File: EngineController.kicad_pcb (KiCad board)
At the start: 4 copper layers, 16 parts, among them U3 LM66200DRLR, U4 MAX77827AEFD+T, U5 SC4215

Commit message: Completed schematics
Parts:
- added 12VLED1: RED_LED, Resistor_SMD:R_0402_1005Metric, F.Cu at (158.8, 71.8)
- added 3V3LED1: BLUE_LED, Resistor_SMD:R_0402_1005Metric, F.Cu at (158.8, 73.8)
- added BOOTJUMPER1: Conn_01x02_Male, Connector_PinHeader_2.54mm:PinHeader_1x02_P2.54mm_Vertical, F.Cu at (149.9, 82.4)
- added C1: 10uF, Capacitor_SMD:C_0402_1005Metric, F.Cu at (164.9, 58.7)
- added C10: 0.1uF, Capacitor_SMD:C_0402_1005Metric, F.Cu at (167.7, 66.6)
- added C11: 0.1uF, Capacitor_SMD:C_0402_1005Metric, F.Cu at (170.6, 58.7)
- added C12: 11pF, Capacitor_SMD:C_0402_1005Metric, F.Cu at (170.6, 60.7)
- added C13: 11pF, Capacitor_SMD:C_0402_1005Metric, F.Cu at (170.6, 62.7)
- added C14: 100nF, Capacitor_SMD:C_0402_1005Metric, F.Cu at (151.7, 127.2)
- added C15: 10uF, Capacitor_SMD:C_0402_1005Metric, F.Cu at (151.7, 129.2)
- added C16: 47nF, Capacitor_SMD:C_0402_1005Metric, F.Cu at (151.7, 131.1)
- added C2: 1uF, Capacitor_SMD:C_0402_1005Metric, F.Cu at (164.9, 60.7)
- added C25: 1uF, Capacitor_SMD:C_0402_1005Metric, F.Cu at (111.6, 97.8)
- added C26: 4.7uF, Capacitor_SMD:C_0402_1005Metric, F.Cu at (111.6, 99.7)
- added C27: 47uF, Capacitor_SMD:C_1206_3216Metric, F.Cu at (96.0, 98.4)
- added C28: 47uF, Capacitor_SMD:C_1206_3216Metric, F.Cu at (96.0, 101.8)
- added C29: 47uF, Capacitor_SMD:C_1206_3216Metric, F.Cu at (96.0, 105.1)
- added C3: 0.1uF, Capacitor_SMD:C_0402_1005Metric, F.Cu at (164.9, 62.7)
- added C30: DNP, Capacitor_SMD:C_1206_3216Metric, F.Cu at (96.0, 108.5)
- added C31: 47uF, Capacitor_SMD:C_1206_3216Metric, F.Cu at (96.0, 111.8)
- added C32: DNP, Capacitor_SMD:C_1206_3216Metric, F.Cu at (101.7, 98.4)
- added C33: 47uF, Capacitor_SMD:C_1206_3216Metric, F.Cu at (101.7, 101.8)
- added C34: 100nF, Capacitor_SMD:C_0402_1005Metric, F.Cu at (111.6, 101.7)
- added C35: 0.1uF, Capacitor_SMD:C_0402_1005Metric, F.Cu at (111.6, 103.7)
- added C36: DNP, Capacitor_SMD:C_1206_3216Metric, F.Cu at (101.7, 105.1)
- added C37: DNP, Capacitor_SMD:C_0805_2012Metric, F.Cu at (112.1, 115.0)
- added C38: DNP, Capacitor_SMD:C_1206_3216Metric, F.Cu at (101.7, 108.5)
- added C39: DNP, Capacitor_SMD:C_1206_3216Metric, F.Cu at (101.7, 111.8)
- added C4: 1uF, Capacitor_SMD:C_0402_1005Metric, F.Cu at (164.9, 64.6)
- added C40: DNP, Capacitor_SMD:C_1206_3216Metric, F.Cu at (107.3, 98.4)
- added C41: DNP, Capacitor_SMD:C_0805_2012Metric, F.Cu at (112.1, 118.0)
- added C42: DNP, Capacitor_SMD:C_1206_3216Metric, F.Cu at (107.3, 101.8)
- added C43: DNP, Capacitor_SMD:C_1206_3216Metric, F.Cu at (107.3, 105.1)
- added C44: DNP, Capacitor_SMD:C_1206_3216Metric, F.Cu at (107.3, 108.5)
- added C45: DNP, Capacitor_SMD:C_1206_3216Metric, F.Cu at (107.3, 111.8)
- added C46: 0.1uF, Capacitor_SMD:C_0402_1005Metric, F.Cu at (155.6, 101.7)
- added C47: 1uF, Capacitor_SMD:C_0402_1005Metric, F.Cu at (114.2, 74.5)
- added C48: 220nF, Capacitor_SMD:C_0402_1005Metric, F.Cu at (114.2, 76.4)
- added C49: 10uF, Capacitor_SMD:C_0603_1608Metric, F.Cu at (130.7, 74.7)
- added C5: 0.1uF, Capacitor_SMD:C_0402_1005Metric, F.Cu at (164.9, 66.6)
- added C50: 0.1uF, Capacitor_SMD:C_0402_1005Metric, F.Cu at (114.2, 78.4)
- added C51: 0.1uF, Capacitor_SMD:C_0402_1005Metric, F.Cu at (114.2, 80.4)
- added C52: 100nF, Capacitor_SMD:C_0603_1608Metric, F.Cu at (130.7, 77.2)
- added C53: 10nF, Capacitor_SMD:C_0402_1005Metric, F.Cu at (114.2, 82.3)
- added C54: 10nF, Capacitor_SMD:C_0402_1005Metric, F.Cu at (114.2, 84.3)
- added C55: 10nF, Capacitor_SMD:C_0402_1005Metric, F.Cu at (114.2, 86.3)
- added C56: 10uF, Capacitor_SMD:C_0603_1608Metric, F.Cu at (136.7, 108.0)
- added C57: 180pF, Capacitor_SMD:C_0402_1005Metric, F.Cu at (117.8, 97.8)
- added C58: 3.9nF, Capacitor_SMD:C_0402_1005Metric, F.Cu at (117.8, 99.7)
- added C59: 1uF, Capacitor_SMD:C_0402_1005Metric, F.Cu at (117.8, 101.7)
- added C6: 0.1uF, Capacitor_SMD:C_0402_1005Metric, F.Cu at (167.7, 58.7)
- added C60: 22uF, Capacitor_SMD:C_0805_2012Metric, F.Cu at (127.2, 108.2)
- added C61: 22uF, Capacitor_SMD:C_0805_2012Metric, F.Cu at (127.2, 111.2)
- added C62: 100nF, Capacitor_SMD:C_0402_1005Metric, F.Cu at (117.8, 103.7)
- added C63: 2.2uF, Capacitor_SMD:C_0402_1005Metric, F.Cu at (117.8, 105.6)
- added C64: 100nF, Capacitor_SMD:C_0402_1005Metric, F.Cu at (117.8, 107.6)
- added C65: 47uF, Capacitor_SMD:C_1206_3216Metric, F.Cu at (119.2, 110.3)
- added C66: 10uF, Capacitor_SMD:C_0402_1005Metric, F.Cu at (120.6, 97.8)
- added C67: 100nF, Capacitor_SMD:C_0402_1005Metric, F.Cu at (120.6, 99.7)
- added C68: 10uF, Capacitor_SMD:C_0603_1608Metric, F.Cu at (136.7, 110.5)
- added C69: 1uF, Capacitor_SMD:C_0402_1005Metric, F.Cu at (120.6, 101.7)
- added C7: 1uF, Capacitor_SMD:C_0402_1005Metric, F.Cu at (167.7, 60.7)
- added C70: 120pF, Capacitor_SMD:C_0402_1005Metric, F.Cu at (120.6, 103.7)
- added C71: 2.2nF, Capacitor_SMD:C_0805_2012Metric, F.Cu at (127.2, 114.2)
- added C72: 22uF, Capacitor_SMD:C_0805_2012Metric, F.Cu at (127.2, 117.3)
- added C73: 2.2uF, Capacitor_SMD:C_0402_1005Metric, F.Cu at (120.6, 105.6)
- added C74: 100nF, Capacitor_SMD:C_0402_1005Metric, F.Cu at (120.6, 107.6)
- added C75: 100nF, Capacitor_SMD:C_0402_1005Metric, F.Cu at (123.5, 97.8)
- added C76: 22uF, Capacitor_SMD:C_1206_3216Metric, F.Cu at (119.2, 113.6)
- added C77: 10uF, Capacitor_SMD:C_0402_1005Metric, F.Cu at (123.5, 99.7)
- added C78: 100nF, Capacitor_SMD:C_0402_1005Metric, F.Cu at (123.5, 101.7)
- added C8: 0.1uF, Capacitor_SMD:C_0402_1005Metric, F.Cu at (167.7, 62.7)
- added C9: 10nF, Capacitor_SMD:C_0402_1005Metric, F.Cu at (167.7, 64.6)
- added D1: SM712_SOT23, Package_TO_SOT_SMD:SOT-23, F.Cu at (155.5, 128.4)
- added D2: SP0503BAHT, Package_TO_SOT_SMD:SOT-143, F.Cu at (161.2, 109.0)
- added ENJUMPER1: Conn_01x02_Male, Connector_PinHeader_2.54mm:PinHeader_1x02_P2.54mm_Vertical, F.Cu at (154.6, 82.4)
- added H1: MountingHole_Pad, MountingHole:MountingHole_3.2mm_M3_DIN965_Pad, F.Cu at (144.0, 61.3)
- added H2: MountingHole_Pad, MountingHole:MountingHole_3.2mm_M3_DIN965_Pad, F.Cu at (144.0, 68.5)
- added H3: MountingHole_Pad, MountingHole:MountingHole_3.2mm_M3_DIN965_Pad, F.Cu at (144.0, 75.6)
- added H4: MountingHole_Pad, MountingHole:MountingHole_3.2mm_M3_DIN965_Pad, F.Cu at (144.0, 82.8)
- added IC1: TPS61089RNRR, iclr:IC_TPS61089RNRR, F.Cu at (136.4, 98.8)
- added IC2: AP2205-W5-7, iclr:SOT95P282X145-5N, F.Cu at (132.0, 109.0)
- added IC3: AP2205-W5-7, iclr:SOT95P282X145-5N, F.Cu at (132.0, 113.7)
- added IC4: TPS61089RNRR, iclr:IC_TPS61089RNRR, F.Cu at (136.4, 102.8)
- added J1: RBUS, Connector_Molex:Molex_Mini-Fit_Jr_5566-06A_2x03_P4.20mm_Vertical, F.Cu at (151.3, 61.0)
- added J2: USB_C_Receptacle_USB2.0, Connector_USB:USB_C_Receptacle_Palconn_UTC16-G, F.Cu at (164.9, 100.9)
- added J3: ServoCH1, Connector_Molex:Molex_Nano-Fit_105313-xx03_1x03_P2.50mm_Horizontal, F.Cu at (142.8, 99.5)
- added J4: ServoCH2, Connector_Molex:Molex_Nano-Fit_105313-xx03_1x03_P2.50mm_Horizontal, F.Cu at (142.8, 110.0)
- added J5: 1053131104, iclr:1053131104, F.Cu at (104.2, 59.8)
- added J6: 1053131104, iclr:1053131104, F.Cu at (119.3, 59.8)
- added J7: 1053131104, iclr:1053131104, F.Cu at (134.4, 59.8)
- added JP1: TermJP, Jumper:SolderJumper-2_P1.3mm_Open_RoundedPad1.0x1.5mm, F.Cu at (156.8, 121.5)
- added JP10: SolderJumper_3_Open, Jumper:SolderJumper-3_P1.3mm_Open_RoundedPad1.0x1.5mm_NumberLabels, F.Cu at (96.0, 93.0)
- added JP2: SolderJumper_3_Open, Jumper:SolderJumper-3_P1.3mm_Open_RoundedPad1.0x1.5mm_NumberLabels, F.Cu at (96.0, 75.2)
- added JP3: SolderJumper_2_Open, Jumper:SolderJumper-2_P1.3mm_Open_RoundedPad1.0x1.5mm, F.Cu at (126.6, 75.2)
- added JP4: SolderJumper_3_Open, Jumper:SolderJumper-3_P1.3mm_Open_RoundedPad1.0x1.5mm_NumberLabels, F.Cu at (96.0, 78.8)
- added JP5: SolderJumper_3_Open, Jumper:SolderJumper-3_P1.3mm_Open_RoundedPad1.0x1.5mm_NumberLabels, F.Cu at (96.0, 82.3)
- added JP6: SolderJumper_2_Open, Jumper:SolderJumper-2_P1.3mm_Open_RoundedPad1.0x1.5mm, F.Cu at (126.6, 78.8)
- added JP7: SolderJumper_3_Open, Jumper:SolderJumper-3_P1.3mm_Open_RoundedPad1.0x1.5mm_NumberLabels, F.Cu at (96.0, 85.9)
- added JP8: SolderJumper_3_Open, Jumper:SolderJumper-3_P1.3mm_Open_RoundedPad1.0x1.5mm_NumberLabels, F.Cu at (96.0, 89.4)
- added JP9: SolderJumper_2_Open, Jumper:SolderJumper-2_P1.3mm_Open_RoundedPad1.0x1.5mm, F.Cu at (126.6, 82.3)
- added L1: 2.0nH, Inductor_SMD:L_0402_1005Metric, F.Cu at (158.8, 75.8)
- added L2: 20nH, Inductor_SMD:L_0402_1005Metric, F.Cu at (158.8, 77.7)
- added Q1: SSM3K15AMFV,L3F, Package_TO_SOT_SMD:SOT-723, F.Cu at (111.6, 106.1)
- added R1: 10K, Resistor_SMD:R_0402_1005Metric, F.Cu at (158.8, 79.7)
- added R10: 60, Resistor_SMD:R_0603_1608Metric, F.Cu at (148.2, 130.0)
- added R11: 60, Resistor_SMD:R_0603_1608Metric, F.Cu at (148.2, 132.5)
- added R12: 5.1k, Resistor_SMD:R_0402_1005Metric, F.Cu at (167.8, 107.7)
- added R13: 5.1k, Resistor_SMD:R_0402_1005Metric, F.Cu at (167.8, 109.7)
- added R14: 5.1k, Resistor_SMD:R_0402_1005Metric, F.Cu at (167.8, 111.7)
- added R19: 10k, Resistor_SMD:R_0402_1005Metric, F.Cu at (94.7, 114.5)
- added R2: 470, Resistor_SMD:R_0402_1005Metric, F.Cu at (161.7, 71.8)
- added R20: 113k, Resistor_SMD:R_0402_1005Metric, F.Cu at (94.7, 116.5)
- added R21: 10k, Resistor_SMD:R_0402_1005Metric, F.Cu at (94.7, 118.5)
- added R22: 2.2, Resistor_SMD:R_0402_1005Metric, F.Cu at (97.6, 114.5)
- added R23: 442k, Resistor_SMD:R_0402_1005Metric, F.Cu at (97.6, 116.5)
- added R24: 1k, Resistor_SMD:R_0402_1005Metric, F.Cu at (97.6, 118.5)
- added R25: 200k, Resistor_SMD:R_0402_1005Metric, F.Cu at (100.5, 114.5)
- added R26: 100k, Resistor_SMD:R_0402_1005Metric, F.Cu at (100.5, 116.5)
- added R27: 10k, Resistor_SMD:R_0402_1005Metric, F.Cu at (100.5, 118.5)
- added R28: 1.5k, Resistor_SMD:R_0402_1005Metric, F.Cu at (155.6, 97.8)
- added R29: 470, Resistor_SMD:R_0402_1005Metric, F.Cu at (155.6, 99.8)
- added R3: 10K, Resistor_SMD:R_0402_1005Metric, F.Cu at (161.7, 73.8)
- added R30: 113k, Resistor_SMD:R_0402_1005Metric, F.Cu at (117.1, 74.5)
- added R31: 40.2k, Resistor_SMD:R_0402_1005Metric, F.Cu at (117.1, 76.5)
- added R32: 1k, Resistor_SMD:R_0402_1005Metric, F.Cu at (117.1, 78.4)
- added R33: 1k, Resistor_SMD:R_0402_1005Metric, F.Cu at (117.1, 80.4)
- added R34: 49k, Resistor_SMD:R_0402_1005Metric, F.Cu at (117.1, 82.4)
- added R35: 113k, Resistor_SMD:R_0402_1005Metric, F.Cu at (117.1, 84.4)
- added R36: 40.2k, Resistor_SMD:R_0402_1005Metric, F.Cu at (120.0, 74.5)
- added R37: 1k, Resistor_SMD:R_0402_1005Metric, F.Cu at (120.0, 76.5)
- added R38: 1k, Resistor_SMD:R_0402_1005Metric, F.Cu at (120.0, 78.4)
- added R39: 49k, Resistor_SMD:R_0402_1005Metric, F.Cu at (120.0, 80.4)
- added R4: 470, Resistor_SMD:R_0402_1005Metric, F.Cu at (161.7, 75.8)
- added R40: 113k, Resistor_SMD:R_0402_1005Metric, F.Cu at (120.0, 82.4)
- added R41: 40.2k, Resistor_SMD:R_0402_1005Metric, F.Cu at (120.0, 84.4)
- added R42: 1k, Resistor_SMD:R_0402_1005Metric, F.Cu at (122.9, 74.5)
- added R43: 1k, Resistor_SMD:R_0402_1005Metric, F.Cu at (122.9, 76.5)
- added R44: 49k, Resistor_SMD:R_0402_1005Metric, F.Cu at (122.9, 78.4)
- added R45: 7.87k, Resistor_SMD:R_0402_1005Metric, F.Cu at (126.4, 97.8)
- added R46: 360k, Resistor_SMD:R_0402_1005Metric, F.Cu at (126.4, 99.8)
- added R47: 100k, Resistor_SMD:R_0402_1005Metric, F.Cu at (126.4, 101.7)
- added R48: 560k, Resistor_SMD:R_0402_1005Metric, F.Cu at (126.4, 103.7)
- added R49: 50k, Resistor_SMD:R_0402_1005Metric, F.Cu at (126.4, 105.7)
- added R5: 499R, Resistor_SMD:R_0402_1005Metric, F.Cu at (161.7, 77.7)
- added R50: 152k, Resistor_SMD:R_0603_1608Metric, F.Cu at (136.7, 113.0)
- added R51: 309k, Resistor_SMD:R_0402_1005Metric, F.Cu at (129.3, 97.8)
- added R52: 18.7k, Resistor_SMD:R_0402_1005Metric, F.Cu at (129.3, 99.8)
- added R53: 976k, Resistor_SMD:R_0402_1005Metric, F.Cu at (129.3, 101.7)
- added R54: 100k, Resistor_SMD:R_0402_1005Metric, F.Cu at (129.3, 103.7)
- added R55: 51k, Resistor_SMD:R_0402_1005Metric, F.Cu at (129.3, 105.7)
- added R56: 442k, Resistor_SMD:R_0402_1005Metric, F.Cu at (132.2, 97.8)
- added R57: 475k, Resistor_SMD:R_0402_1005Metric, F.Cu at (132.2, 99.8)
- added R58: 287k, Resistor_SMD:R_0402_1005Metric, F.Cu at (132.2, 101.7)
- added R6: 3k, Resistor_SMD:R_0402_1005Metric, F.Cu at (161.7, 79.7)
- added R7: 1.5k, Resistor_SMD:R_0402_1005Metric, F.Cu at (164.6, 71.8)
- added R8: 2.2k, Resistor_SMD:R_0402_1005Metric, F.Cu at (164.6, 73.8)
- added R9: 0, Resistor_SMD:R_0603_1608Metric, F.Cu at (148.2, 127.5)
- added TP1: TestPoint, TestPoint:TestPoint_Pad_D1.0mm, F.Cu at (158.9, 82.3)
- added TP2: TestPoint, TestPoint:TestPoint_Pad_D1.0mm, F.Cu at (158.9, 85.3)
- added TP3: TestPoint, TestPoint:TestPoint_Pad_D1.0mm, F.Cu at (164.9, 108.3)
- added TP4: TestPoint, TestPoint:TestPoint_Pad_D1.0mm, F.Cu at (164.9, 111.3)
- added TP5: TestPoint, TestPoint:TestPoint_Pad_D1.5mm, F.Cu at (142.4, 121.5)
- added TP6: TestPoint, TestPoint:TestPoint_Pad_D1.5mm, F.Cu at (142.4, 125.1)
- added TP7: TestPoint, TestPoint:TestPoint_Pad_D1.5mm, F.Cu at (142.4, 128.6)
- added TP8: TestPoint, TestPoint:TestPoint_Pad_D1.5mm, F.Cu at (142.4, 132.2)
- added TXLED1: GREEN_LED, Resistor_SMD:R_0402_1005Metric, F.Cu at (164.6, 75.8)
- added U1: ESP32-S3, iclr:QFN40P700X700X90-57N, F.Cu at (152.7, 75.4)
- added U2: SN65HVD230, Package_SO:SOIC-8_3.9x4.9mm_P1.27mm, F.Cu at (150.4, 123.0)
- added U6: SiC437BED-T1-GE3, iclr:SiC437BEDT1GE3, F.Cu at (106.0, 117.4)
- added U7: ADS131M06IRSNR, iclr:ADS131M06IRSNR, F.Cu at (105.2, 81.1)
- added USBLED1: WHITE_LED, Resistor_SMD:R_0402_1005Metric, F.Cu at (167.8, 113.7)
- added Y1: R940000171, Crystal:Crystal_SMD_2016-4Pin_2.0x1.6mm, F.Cu at (162.3, 82.6)
- renumbered C20 to C17, C21 to C18, C22 to C19, C23 to C20, C24 to C21, C25 to C22, C26 to C23, C27 to C24, R14 to R15, R15 to R16, R16 to R17, R17 to R18

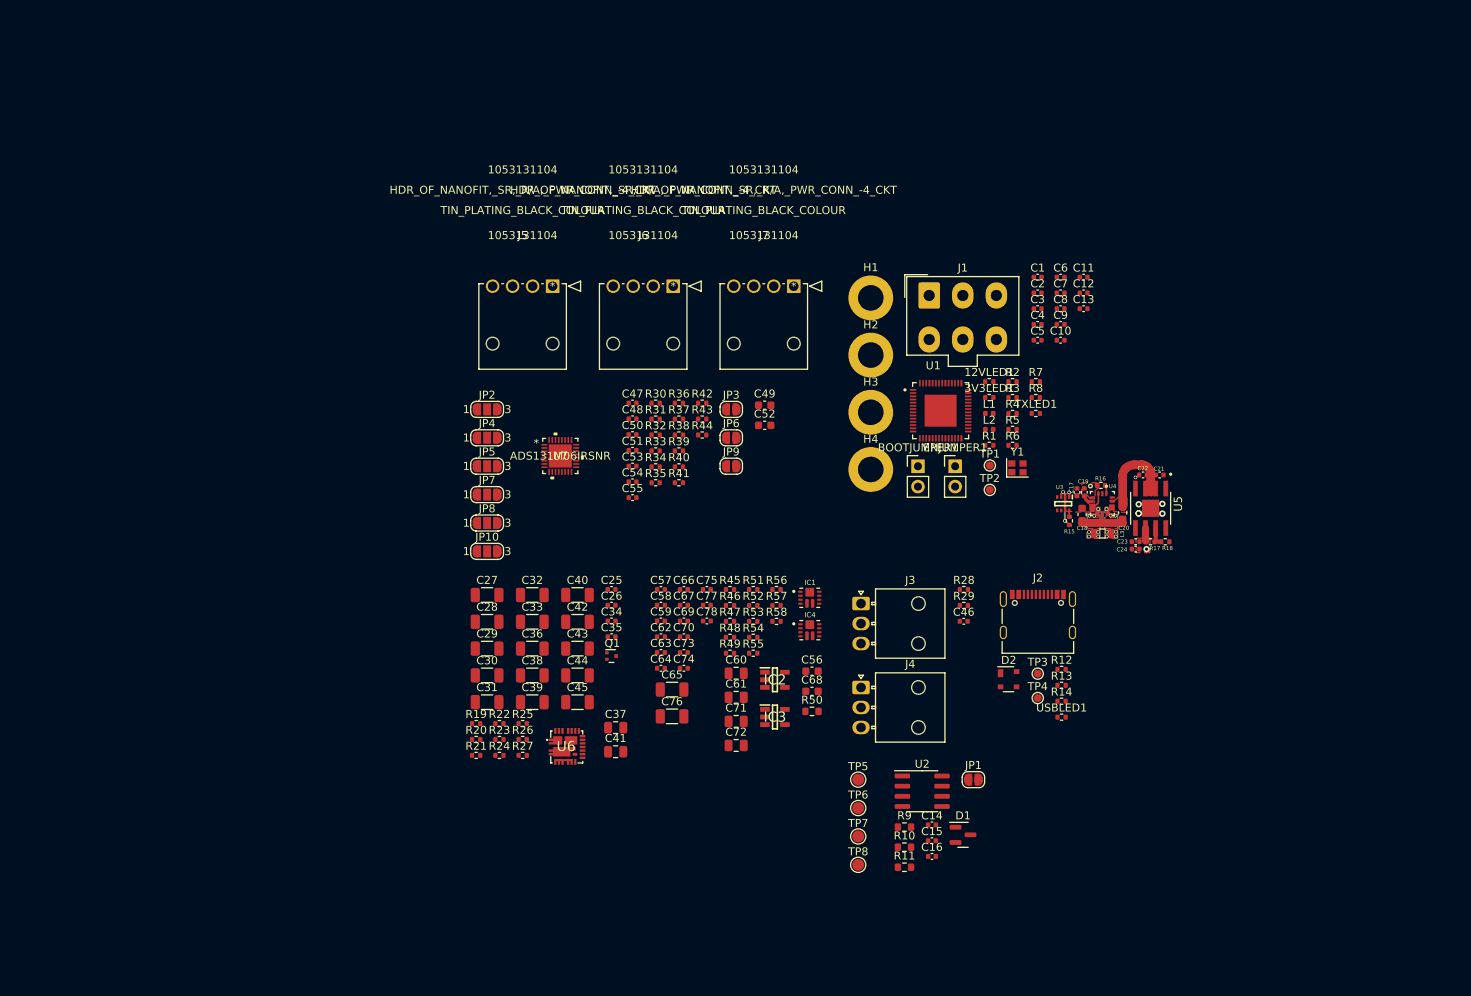
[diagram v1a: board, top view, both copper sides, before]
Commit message: forgot sd card and added ads chip
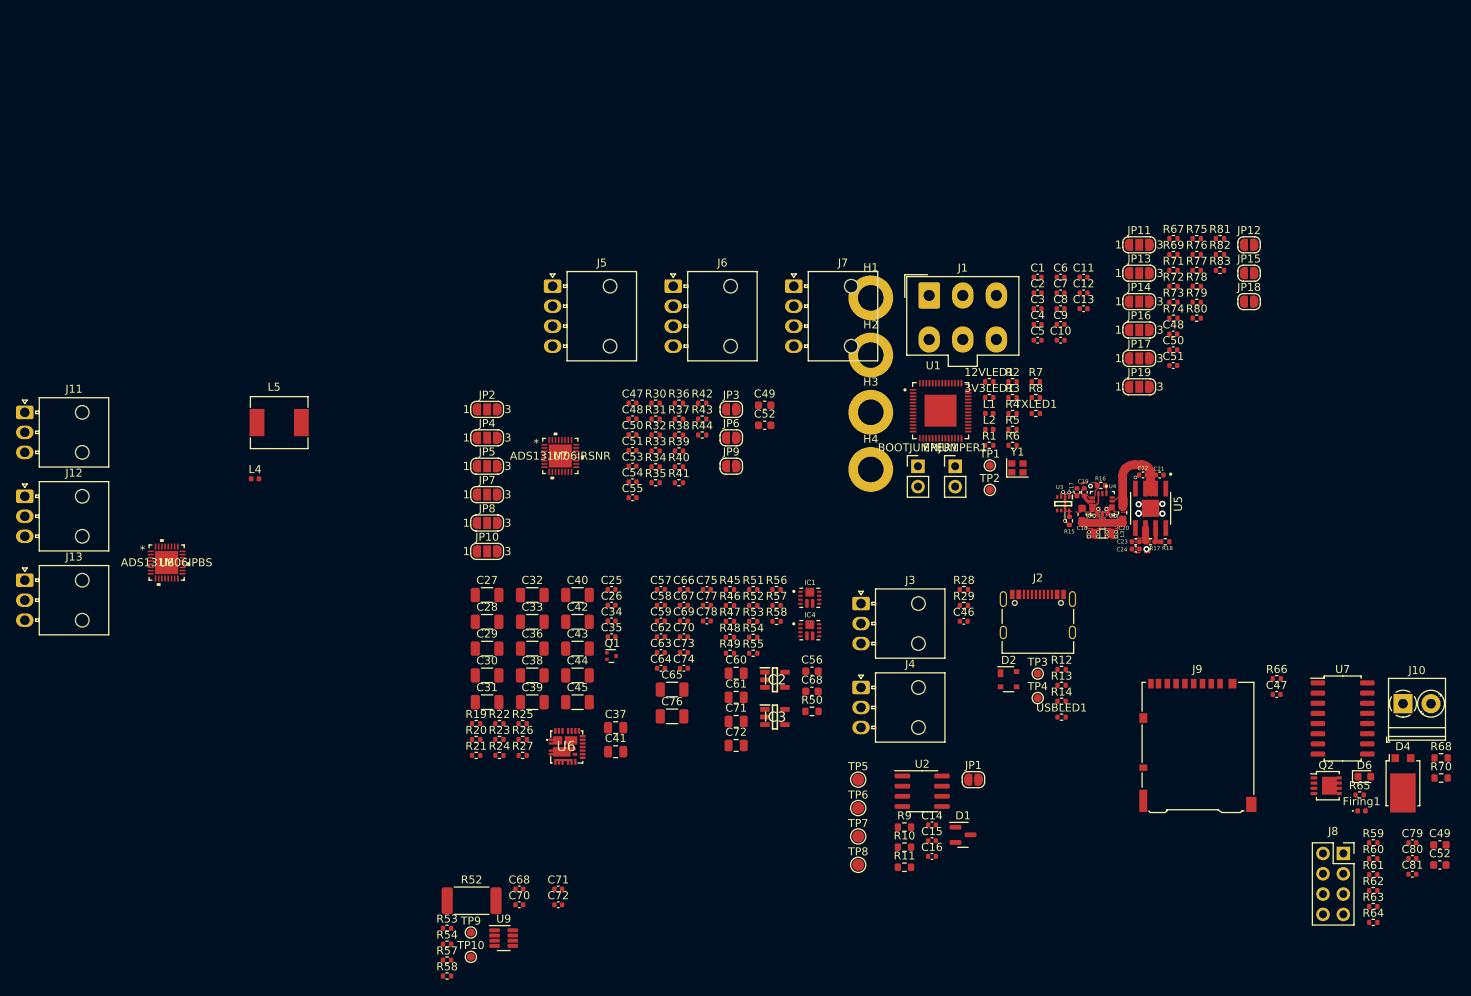
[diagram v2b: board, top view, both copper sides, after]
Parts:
- added C47: 0.1uF, Capacitor_SMD:C_0402_1005Metric, F.Cu at (194.7, 110.9)
- added C48: 10nF, Capacitor_SMD:C_0402_1005Metric, F.Cu at (181.8, 65.8)
- added C49: 10uF, Capacitor_SMD:C_0603_1608Metric, F.Cu at (215.1, 129.7)
- added C50: 10nF, Capacitor_SMD:C_0402_1005Metric, F.Cu at (181.8, 67.8)
- added C51: 10nF, Capacitor_SMD:C_0402_1005Metric, F.Cu at (181.8, 69.8)
- added C52: 100nF, Capacitor_SMD:C_0603_1608Metric, F.Cu at (215.1, 132.2)
- added C68: 0.1uF, Capacitor_SMD:C_0402_1005Metric, F.Cu at (100.1, 135.2)
- added C70: 0.1uF, Capacitor_SMD:C_0402_1005Metric, F.Cu at (100.1, 137.2)
- added C71: 1uF, Capacitor_SMD:C_0402_1005Metric, F.Cu at (104.9, 135.2)
- added C72: 1uF, Capacitor_SMD:C_0402_1005Metric, F.Cu at (104.9, 137.2)
- added C79: 1uF, Capacitor_SMD:C_0402_1005Metric, F.Cu at (211.7, 129.4)
- added C80: 1uF, Capacitor_SMD:C_0402_1005Metric, F.Cu at (211.7, 131.4)
- added C81: 220nF, Capacitor_SMD:C_0402_1005Metric, F.Cu at (211.7, 133.3)
- added D4: DST1550S, Package_TO_SOT_SMD:TO-277B, F.Cu at (210.5, 122.0)
- added D6: RED_LED, LED_SMD:LED_0603_1608Metric, F.Cu at (205.7, 121.2)
- added Firing1: EMERALD_LED, LED_SMD:LED_0402_1005Metric, F.Cu at (205.3, 125.4)
- added J10: Conn_01x02_Male, TerminalBlock_Phoenix:TerminalBlock_Phoenix_PT-1,5-2-3.5-H_1x02_P3.50mm_Horizontal, F.Cu at (210.5, 112.0)
- added J11: 1053131104, Connector_Molex:Molex_Nano-Fit_105313-xx03_1x03_P2.50mm_Horizontal, F.Cu at (38.3, 75.6)
- added J12: 1053131104, Connector_Molex:Molex_Nano-Fit_105313-xx03_1x03_P2.50mm_Horizontal, F.Cu at (38.3, 86.1)
- added J13: 1053131104, Connector_Molex:Molex_Nano-Fit_105313-xx03_1x03_P2.50mm_Horizontal, F.Cu at (38.3, 96.6)
- added J8: GPIO Breakout, Connector_PinSocket_2.54mm:PinSocket_2x04_P2.54mm_Vertical, F.Cu at (203.1, 130.8)
- added J9: Micro_SD_Card_Det, Connector_Card:microSD_HC_Hirose_DM3AT-SF-PEJM5, F.Cu at (184.9, 117.2)
- added JP11: SolderJumper_3_Open, Jumper:SolderJumper-3_P1.3mm_Open_RoundedPad1.0x1.5mm_NumberLabels, F.Cu at (177.6, 54.7)
- added JP12: SolderJumper_2_Open, Jumper:SolderJumper-2_P1.3mm_Open_RoundedPad1.0x1.5mm, F.Cu at (191.3, 54.7)
- added JP13: SolderJumper_3_Open, Jumper:SolderJumper-3_P1.3mm_Open_RoundedPad1.0x1.5mm_NumberLabels, F.Cu at (177.6, 58.2)
- added JP14: SolderJumper_3_Open, Jumper:SolderJumper-3_P1.3mm_Open_RoundedPad1.0x1.5mm_NumberLabels, F.Cu at (177.6, 61.8)
- added JP15: SolderJumper_2_Open, Jumper:SolderJumper-2_P1.3mm_Open_RoundedPad1.0x1.5mm, F.Cu at (191.3, 58.2)
- added JP16: SolderJumper_3_Open, Jumper:SolderJumper-3_P1.3mm_Open_RoundedPad1.0x1.5mm_NumberLabels, F.Cu at (177.6, 65.3)
- added JP17: SolderJumper_3_Open, Jumper:SolderJumper-3_P1.3mm_Open_RoundedPad1.0x1.5mm_NumberLabels, F.Cu at (177.6, 68.9)
- added JP18: SolderJumper_2_Open, Jumper:SolderJumper-2_P1.3mm_Open_RoundedPad1.0x1.5mm, F.Cu at (191.3, 61.8)
- added JP19: SolderJumper_3_Open, Jumper:SolderJumper-3_P1.3mm_Open_RoundedPad1.0x1.5mm_NumberLabels, F.Cu at (177.6, 72.4)
- added L4: 3.3uH, Inductor_SMD:L_0402_1005Metric, F.Cu at (67.0, 83.9)
- added L5: SRR6038-5R0Y, iclr:IND_SRP6540-390M, F.Cu at (70.1, 76.9)
- added Q2: BUK9M11-40EX, Package_TO_SOT_SMD:LFPAK33, F.Cu at (200.9, 122.3)
- added R52: 2m, Resistor_SMD:R_2512_6332Metric_Pad1.40x3.35mm_HandSolder, F.Cu at (94.1, 136.7)
- added R53: 10, Resistor_SMD:R_0402_1005Metric, F.Cu at (91.0, 140.1)
- added R54: 10, Resistor_SMD:R_0402_1005Metric, F.Cu at (91.0, 142.1)
- added R57: 3.3k, Resistor_SMD:R_0402_1005Metric, F.Cu at (91.0, 144.1)
- added R58: 3.3k, Resistor_SMD:R_0402_1005Metric, F.Cu at (91.0, 146.1)
- added R59: DNP, Resistor_SMD:R_0402_1005Metric, F.Cu at (206.8, 129.4)
- added R60: DNP, Resistor_SMD:R_0402_1005Metric, F.Cu at (206.8, 131.4)
- added R61: DNP, Resistor_SMD:R_0402_1005Metric, F.Cu at (206.8, 133.4)
- added R62: DNP, Resistor_SMD:R_0402_1005Metric, F.Cu at (206.8, 135.4)
- added R63: DNP, Resistor_SMD:R_0402_1005Metric, F.Cu at (206.8, 137.4)
- added R64: DNP, Resistor_SMD:R_0402_1005Metric, F.Cu at (206.8, 139.4)
- added R65: 120, Resistor_SMD:R_0402_1005Metric, F.Cu at (205.1, 123.4)
- added R66: 10k, Resistor_SMD:R_0402_1005Metric, F.Cu at (194.8, 108.9)
- added R67: 113k, Resistor_SMD:R_0402_1005Metric, F.Cu at (181.8, 53.9)
- added R68: 120, Resistor_SMD:R_0603_1608Metric, F.Cu at (215.3, 118.8)
- added R69: 40.2k, Resistor_SMD:R_0402_1005Metric, F.Cu at (181.8, 55.9)
- added R70: 10k, Resistor_SMD:R_0603_1608Metric, F.Cu at (215.3, 121.3)
- added R71: 1k, Resistor_SMD:R_0402_1005Metric, F.Cu at (181.8, 57.9)
- added R72: 1k, Resistor_SMD:R_0402_1005Metric, F.Cu at (181.8, 59.9)
- added R73: 49k, Resistor_SMD:R_0402_1005Metric, F.Cu at (181.8, 61.9)
- added R74: 113k, Resistor_SMD:R_0402_1005Metric, F.Cu at (181.8, 63.8)
- added R75: 40.2k, Resistor_SMD:R_0402_1005Metric, F.Cu at (184.7, 53.9)
- added R76: 1k, Resistor_SMD:R_0402_1005Metric, F.Cu at (184.7, 55.9)
- added R77: 1k, Resistor_SMD:R_0402_1005Metric, F.Cu at (184.7, 57.9)
- added R78: 49k, Resistor_SMD:R_0402_1005Metric, F.Cu at (184.7, 59.9)
- added R79: 113k, Resistor_SMD:R_0402_1005Metric, F.Cu at (184.7, 61.9)
- added R80: 40.2k, Resistor_SMD:R_0402_1005Metric, F.Cu at (184.7, 63.8)
- added R81: 1k, Resistor_SMD:R_0402_1005Metric, F.Cu at (187.7, 53.9)
- added R82: 1k, Resistor_SMD:R_0402_1005Metric, F.Cu at (187.7, 55.9)
- added R83: 49k, Resistor_SMD:R_0402_1005Metric, F.Cu at (187.7, 57.9)
- added TP10: TestPoint, TestPoint:TestPoint_Pad_D1.0mm, F.Cu at (94.0, 143.7)
- added TP9: TestPoint, TestPoint:TestPoint_Pad_D1.0mm, F.Cu at (94.0, 140.6)
- added U7: LTV-247, Package_SO:SOP-16_4.4x10.4mm_P1.27mm, F.Cu at (203.0, 113.9)
- added U8: ADS131M06IPBS, iclr:ADS131M06IRSNR, F.Cu at (56.0, 94.4)
- added U9: INA219AxDCN, Package_TO_SOT_SMD:SOT-23-8, F.Cu at (98.1, 141.3)
- J5, J6, J7: footprint iclr:1053131104 -> Connector_Molex:Molex_Nano-Fit_105313-xx04_1x04_P2.50mm_Horizontal
- R20: value 113k -> 130k
- R23: value 442k -> 294k
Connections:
- C77 pad 1: /Boosts/LDO11V_IN -> /Boosts/LDO13V_IN
- C78 pad 1: /Boosts/LDO11V_IN -> /Boosts/LDO13V_IN
- U1 pad 10: unconnected-(U1-GPIO5/ADC1_CH4-Pad10) -> /GPIO5
- U1 pad 11: unconnected-(U1-GPIO6/ADC1_CH5-Pad11) -> /GPIO3
- U1 pad 12: unconnected-(U1-GPIO7/ADC1_CH6-Pad12) -> /GPIO1
- U1 pad 13: unconnected-(U1-GPIO8/ADC1_CH7-Pad13) -> /GPIO2
- U1 pad 14: unconnected-(U1-GPIO9/ADC1_CH8-Pad14) -> /GPIO0
- U1 pad 15: unconnected-(U1-GPIO10/ADC1_CH9-Pad15) -> /Servo2PWM
- U1 pad 16: unconnected-(U1-GPIO11/ADC2_CH0-Pad16) -> /Servo1PWM
- U1 pad 17: unconnected-(U1-GPIO12/ADC2_CH1-Pad17) -> /ServoV_LOG
- U1 pad 28: unconnected-(U1-SPI_CS1/GPIO26-Pad28) -> /Nuke 1
- U1 pad 30: unconnected-(U1-SPIHD/GPIO27-Pad30) -> /Cont 1
- U1 pad 31: unconnected-(U1-SPIWP/GPIO28-Pad31) -> /VSPI_MOSI
- U1 pad 32: unconnected-(U1-SPICS0/GPIO29-Pad32) -> /VSPI_SCLK
- U1 pad 33: unconnected-(U1-SPICLK/GPIO30-Pad33) -> /VSPI_MISO
- U1 pad 34: unconnected-(U1-SPIQ/GPIO31-Pad34) -> /SD1_CS
- U1 pad 38: /CAN_TX -> /HSPI_MOSI
- U1 pad 39: /CAN_RX -> /HSPI_SCLK
- U1 pad 40: /ServoV_LOG -> /HSPI_MISO
- U1 pad 41: /Servo1PWM -> unconnected-(U1-GPIO36-Pad41)
- U1 pad 42: /Servo2PWM -> unconnected-(U1-GPIO37-Pad42)
- U1 pad 43: /BUCK_EN -> unconnected-(U1-GPIO38-Pad43)
- U1 pad 6: unconnected-(U1-GPIO1/ADC1_CH0-Pad6) -> /CAN_RX
- U1 pad 7: unconnected-(U1-GPIO2/ADC1_CH1-Pad7) -> /CAN_TX
- U1 pad 9: unconnected-(U1-GPIO4/ADC1_CH3-Pad9) -> /GPIO4

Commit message: update
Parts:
- removed the C47 at (194.7, 110.9)
- removed the C47 at (114.2, 74.5)
- removed the C48 at (114.2, 76.4)
- removed the C48 at (181.8, 65.8)
- removed the C49 at (130.7, 74.7)
- removed the C50 at (114.2, 78.4)
- removed the C50 at (181.8, 67.8)
- removed the C51 at (181.8, 69.8)
- removed the C51 at (114.2, 80.4)
- removed the C52 at (130.7, 77.2)
- removed C68: 10uF, Capacitor_SMD:C_0603_1608Metric
- removed C68, C70: 0.1uF, Capacitor_SMD:C_0402_1005Metric
- removed C70: 120pF, Capacitor_SMD:C_0402_1005Metric
- removed the C71 at (127.2, 114.2)
- removed the C71 at (104.9, 135.2)
- removed the C72 at (104.9, 137.2)
- removed the C72 at (127.2, 117.3)
- removed R52: 18.7k, Resistor_SMD:R_0402_1005Metric
- removed R52: 2m, Resistor_SMD:R_2512_6332Metric_Pad1.40x3.35mm_HandSolder
- removed R53: 976k, Resistor_SMD:R_0402_1005Metric
- removed R53, R54: 10, Resistor_SMD:R_0402_1005Metric
- removed R54: 100k, Resistor_SMD:R_0402_1005Metric
- removed R57, R58: 3.3k, Resistor_SMD:R_0402_1005Metric
- removed R57: 475k, Resistor_SMD:R_0402_1005Metric
- removed R58: 287k, Resistor_SMD:R_0402_1005Metric
- removed TP10, TP9: TestPoint, TestPoint:TestPoint_Pad_D1.0mm
- removed the U7 at (105.2, 81.1)
- removed U9: INA219AxDCN, Package_TO_SOT_SMD:SOT-23-8
- added C47: 0.1uF, Capacitor_SMD:C_0402_1005Metric, F.Cu at (188.6, 105.2)
- added C48: 10nF, Capacitor_SMD:C_0402_1005Metric, F.Cu at (132.9, 131.1)
- added C50: 10nF, Capacitor_SMD:C_0402_1005Metric, F.Cu at (132.9, 133.1)
- added C51: 10nF, Capacitor_SMD:C_0402_1005Metric, F.Cu at (132.9, 135.1)
- added C71: 1uF, Capacitor_SMD:C_0402_1005Metric, F.Cu at (178.1, 51.4)
- added C72: 1uF, Capacitor_SMD:C_0402_1005Metric, F.Cu at (185.1, 51.1)
- added C82: 22uF, Capacitor_SMD:C_1206_3216Metric, F.Cu at (195.6, 53.0)
- added L6: SRR6038-5R0Y, iclr:IND_SRP6540-390M, F.Cu at (193.2, 47.8)
- added R84: 18.7k, Resistor_SMD:R_0402_1005Metric, F.Cu at (186.2, 54.7)
- added R85: 953k, Resistor_SMD:R_0402_1005Metric, F.Cu at (185.7, 53.2)
- added R86: 118k, Resistor_SMD:R_0402_1005Metric, F.Cu at (185.7, 52.1)
- added R87: 475k, Resistor_SMD:R_0402_1005Metric, F.Cu at (191.2, 53.4)
- added R88: 287k, Resistor_SMD:R_0402_1005Metric, F.Cu at (187.7, 51.1)
- C74: value 100nF -> 10uF
- C76: value 22uF -> 10uF; footprint Capacitor_SMD:C_1206_3216Metric -> Capacitor_SMD:C_0603_1608Metric
- C77: value 10uF -> 120pF
- C78: value 100nF -> 2.2nF; footprint Capacitor_SMD:C_0402_1005Metric -> Capacitor_SMD:C_0805_2012Metric
- C79: value 1uF -> 22uF; footprint Capacitor_SMD:C_0402_1005Metric -> Capacitor_SMD:C_0805_2012Metric
- C80: value 1uF -> 100nF
- C81: value 220nF -> 100nF
- J11, J12, J13: footprint Connector_Molex:Molex_Nano-Fit_105313-xx03_1x03_P2.50mm_Horizontal -> Connector_Molex:Molex_Nano-Fit_105313-xx04_1x04_P2.50mm_Horizontal
- R56: value 442k -> 360k
- moved J13 160.6 mm to (187.2, 36.6), turned to 90 degrees
- moved J12 140.7 mm to (170.0, 36.8), turned to 90 degrees
- moved U8 132.9 mm to (181.5, 50.6), turned to -90 degrees
- moved J11 122.7 mm to (159.3, 56.0), turned to 180 degrees
- moved L4 112.9 mm to (179.5, 74.5), turned to 180 degrees
- moved JP15 106.2 mm to (114.7, 131.9)
- moved JP12 106.2 mm to (114.7, 128.3)
- moved JP18 106.2 mm to (114.7, 135.4)
- moved L5 103.1 mm to (170.5, 53.9), turned to 180 degrees
- moved R21 101.7 mm to (183.1, 68.2), turned to -90 degrees
- moved R69 101.2 mm to (124.2, 139.1)
- moved R76 101.2 mm to (127.1, 139.1)
- moved R82 101.2 mm to (130.0, 139.1)
- moved R67 101.2 mm to (124.2, 137.1)
- moved R75 101.2 mm to (127.1, 137.1)
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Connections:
- C69 pad 1: /Boosts/LDO13V_IN -> /Boosts/LDO11V_IN
- C73 pad 1: +12V -> /Boosts/10V
- C74 pad 1: Net-(IC4-BOOT) -> /Boosts/LDO11V_IN
- C74 pad 2: Net-(IC4-SW) -> GND
- C75 pad 1: +3V3 -> /Boosts/LDO11V_IN
- C76 pad 1: +3V3 -> Net-(IC4-EN)
- C77 pad 1: /Boosts/LDO13V_IN -> Net-(IC4-COMP)
- C78 pad 1: /Boosts/LDO13V_IN -> Net-(C78-Pad1)
- C79 pad 1: GND -> /Boosts/LDO11V_IN
- C79 pad 2: +3V3 -> GND
- C80 pad 1: GND -> Net-(IC4-BOOT)
- C80 pad 2: +3V3 -> Net-(IC4-SW)
- C81 pad 1: Net-(IC5-CAP) -> +3V3
- IC3 pad 1: /Boosts/LDO13V_IN -> /Boosts/LDO11V_IN
- IC3 pad 3: /Boosts/LDO13V_IN -> /Boosts/LDO11V_IN
- IC3 pad 5: +12V -> /Boosts/10V
- IC4 pad 1: /Boosts/SW_12V -> /Boosts/SW_10V
- IC4 pad 3: /Boosts/FB_12V -> /Boosts/FB_10V
- IC4 pad 6: /Boosts/LDO13V_IN -> /Boosts/LDO11V_IN
- R56 pad 2: +12V -> /Boosts/10V
- U1 pad 18: /MISO -> /BUCK_EN
- U1 pad 19: /MOSI -> unconnected-(U1-GPIO14/ADC2_CH3-Pad19)
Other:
- board outline added: 50 x 100 mm
